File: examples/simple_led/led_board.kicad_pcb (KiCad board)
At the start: 2 copper layers, 25 x 20 mm, 5 parts, among them J1 +5V_GND

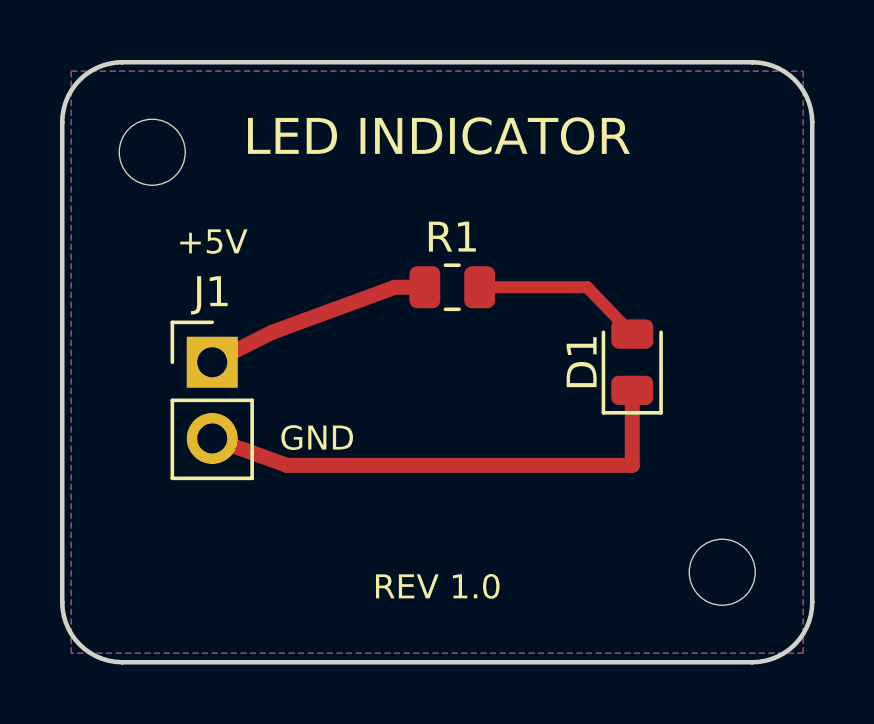
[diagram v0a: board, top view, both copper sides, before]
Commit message: docs: comprehensive README for rf-ai-suite with Simple LED automated pipeline and 3D raytrace render
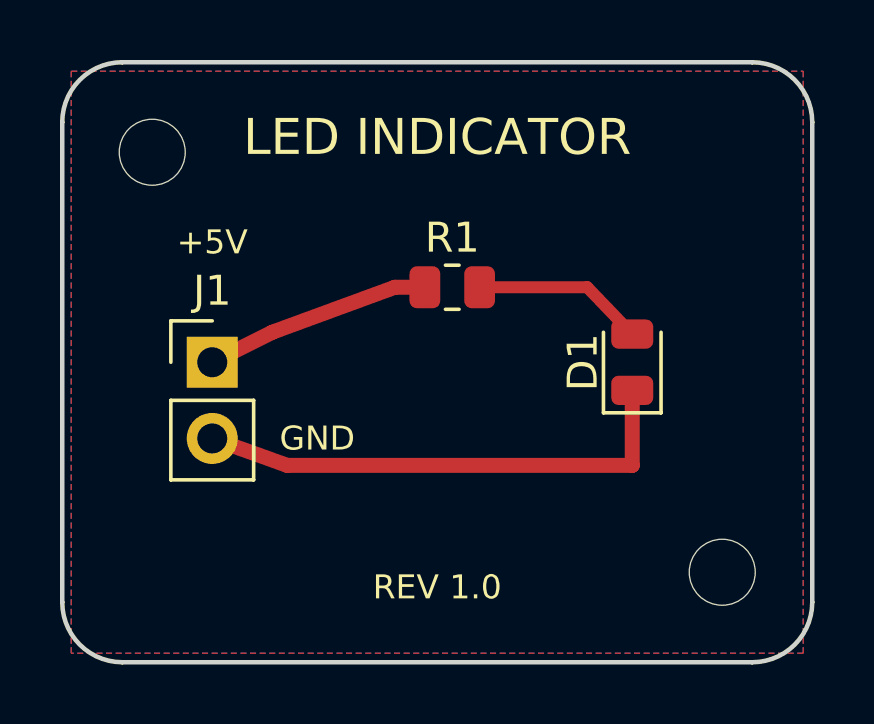
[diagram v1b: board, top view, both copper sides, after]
